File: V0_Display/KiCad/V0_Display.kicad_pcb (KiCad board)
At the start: 2 copper layers, 80 x 35 mm, 28 parts, among them J1 USB_B_Micro, J2 I2C Header 1, J3 Conn_01x03, J4 Conn_01x02, J5 SWD Header, J7 USB_Header, J8 Conn_01x02, SW5 SW_SPST, SW6 SW_SPST, SW7 Rotary_Encoder_Switch, U1 AP2127K-3.3, U2 STM32F042F6Px, U3 74LVC1G17

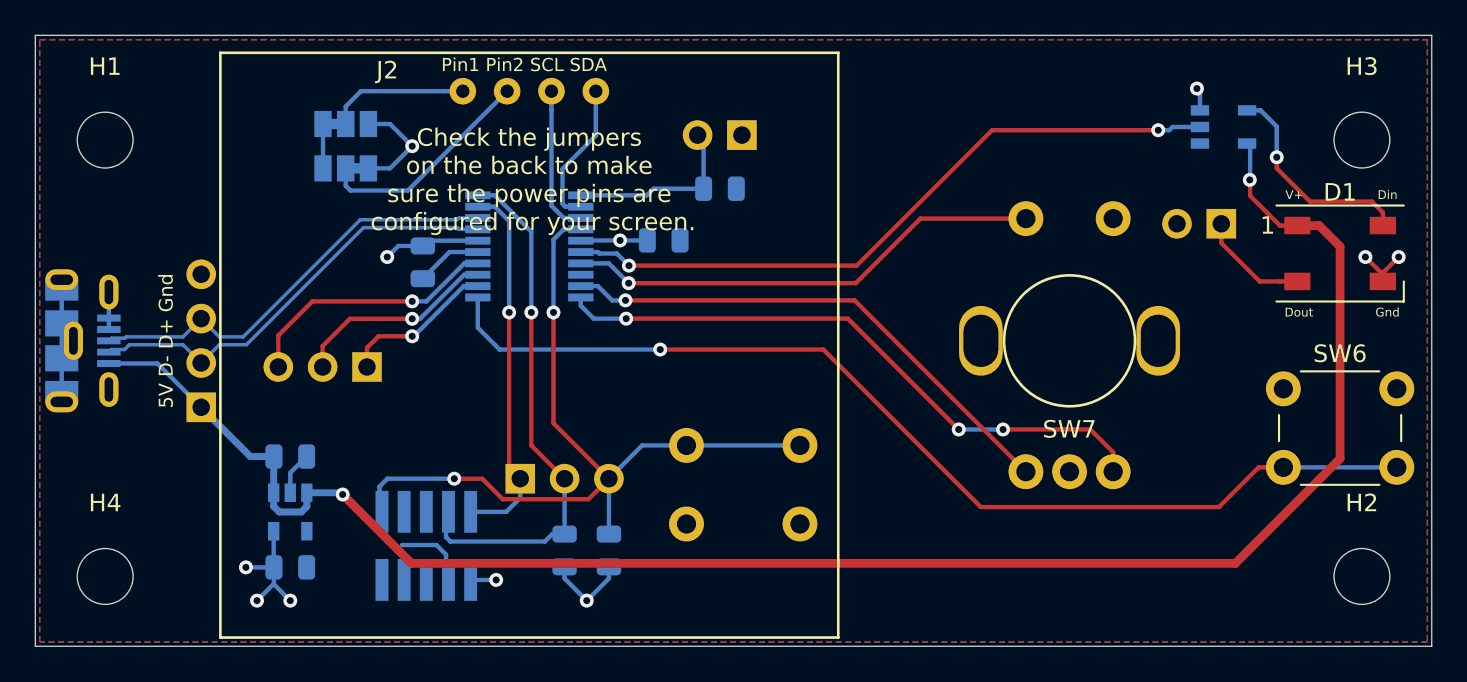
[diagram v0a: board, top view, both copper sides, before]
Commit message: Create Atmega328p version of the V0 Display
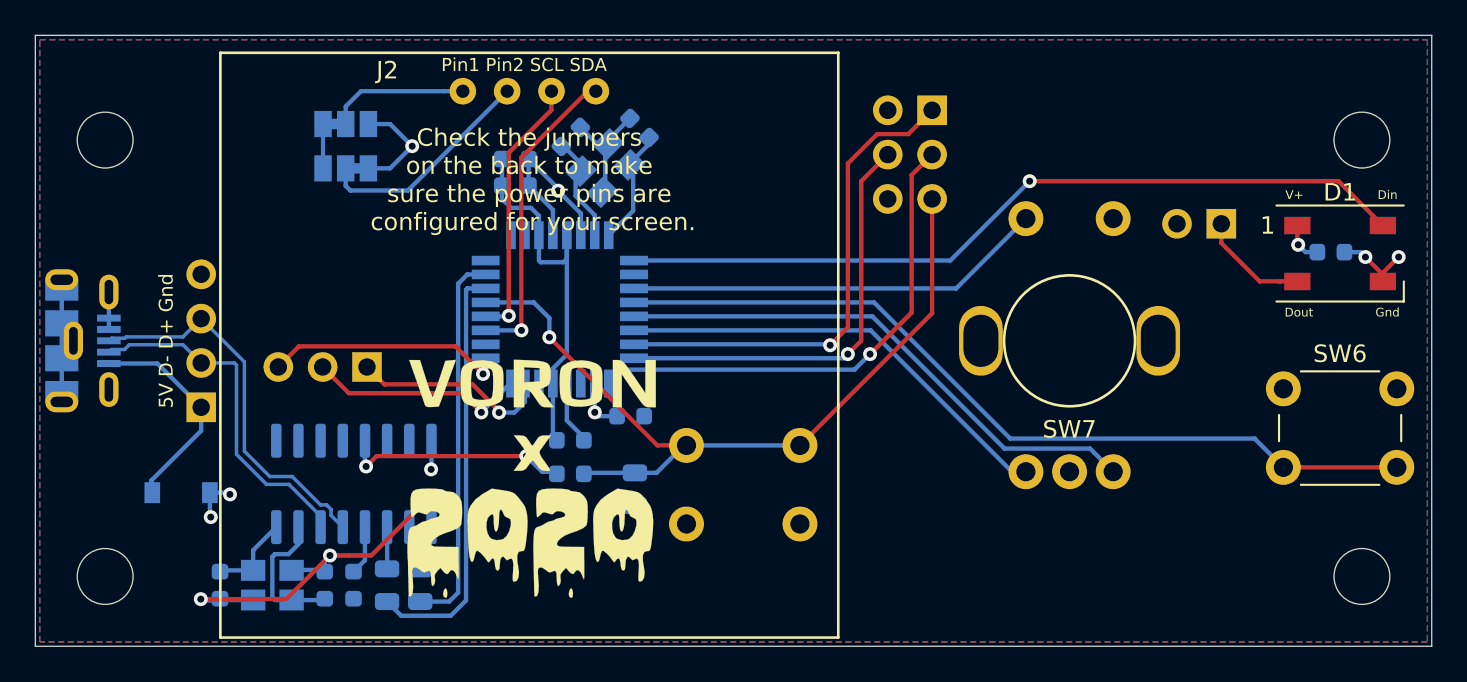
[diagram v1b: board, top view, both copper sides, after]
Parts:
- removed J4: Conn_01x02, V0-Display:PinHeader_1x02_P2.54mm_Vertical
- removed J5: SWD Header, V0-Display:PinHeader_2x05_P1.27mm_Vertical_SMD
- removed R2: 10K, V0-Display:R_0805_2012Metric
- removed U1: AP2127K-3.3, V0-Display:SOT-23-5
- removed U2: STM32F042F6Px, V0-Display:TSSOP-20_4.4x6.5mm_P0.65mm
- removed U3: 74LVC1G17, V0-Display:SOT-753
- added C10: 0.1uF, V0-Display:C_0603_1608Metric, B.Cu at (159.4, 62.1)
- added C11: 0.1uF, V0-Display:C_0603_1608Metric, B.Cu at (103.4, 81.2)
- added C5: 22pF, V0-Display:C_0603_1608Metric, B.Cu at (101.8, 81.2)
- added C6: 22pF, V0-Display:C_0603_1608Metric, B.Cu at (95.8, 81.2)
- added C7: 22pF, V0-Display:C_0603_1608Metric, B.Cu at (119.8, 55.0)
- added C8: 22pF, V0-Display:C_0603_1608Metric, B.Cu at (115.8, 55.5)
- added C9: 0.1uF, V0-Display:C_0603_1608Metric, B.Cu at (119.3, 71.5)
- added D2: 5819, V0-Display:D_SOD-123, B.Cu at (93.5, 75.8)
- added G***: LOGO, V0-Display:2020, F.Cu at (113.7, 74.5)
- added R4: 1K, V0-Display:R_0805_2012Metric, B.Cu at (107.2, 81.2)
- added U4: ATmega328P-AU, V0-Display:TQFP-32_7x7mm_P0.8mm, B.Cu at (115.2, 65.3)
- added U5: CH340G, V0-Display:SOIC-16_3.9x9.9mm_P1.27mm, B.Cu at (103.4, 75.3)
- added Y1: 12MHz, V0-Display:Crystal_SMD_3225-4Pin_3.2x2.5mm, B.Cu at (98.8, 81.2)
- added Y2: 16MHz, V0-Display:Crystal_SMD_3225-4Pin_3.2x2.5mm, B.Cu at (117.8, 57.2)
- C1, C2: value 4.7uF -> 0.1uF; footprint V0-Display:C_0805_2012Metric -> V0-Display:C_0603_1608Metric
- C3, C4: footprint V0-Display:C_0805_2012Metric -> V0-Display:C_0603_1608Metric
- J3: value Conn_01x03 -> ICSP; footprint V0-Display:PinHeader_1x03_P2.54mm_Vertical -> V0-Display:PinHeader_2x03_P2.54mm_Vertical
- R3: value 10K -> 1K
- moved J3 31.7 mm to (136.5, 53.9), turned to 180 degrees
- moved C2 17.6 mm to (115.8, 72.8), turned to 180 degrees
- moved C1 16.1 mm to (115.8, 74.8)
- moved R3 10.4 mm to (105.3, 81.2)
- moved C4 9.06 mm to (112.7, 58.3), turned to 180 degrees
- moved C3 7.94 mm to (112.7, 56.7), turned to 0 degrees
- moved R1 3.82 mm to (119.5, 75.7)
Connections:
- C1 pad 1: VBUS -> Net-(C1-Pad1)
- C1 pad 2: GND -> ~Reset
- C2 pad 1: +3V3 -> Net-(C2-Pad1)
- C3 pad 2: +3V3 -> +5V
- C4 pad 1: +3V3 -> +5V
- D1 pad 1: VBUS -> +5V
- D1 pad 4: Net-(D1-Pad4) -> NeoPixel
- J3 pad 1: SWDIO -> MISO
- J3 pad 2: SWDCLK -> +5V
- J3 pad 3: ~Reset -> SCK
- JP1 pad 1: +3V3 -> +5V
- JP2 pad 3: +3V3 -> +5V
- R1 pad 1: +3V3 -> +5V
- R3 pad 1: +3V3 -> Net-(R3-Pad1)
- R3 pad 2: SWDCLK -> RXD
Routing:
- net VBUS: track 102.4 -> 12.3 mm, vias 2 -> 0
- net GND: track 28.7 -> 85.9 mm, vias 3 -> 5
- net SWDCLK: track 30.6 -> 0.00 mm, vias 1 -> 0
- net +3V3: track 29.3 -> 0.00 mm, vias 8 -> 0
- net SCK: track 0.00 -> 28.6 mm, vias 0 -> 1
- net MISO: track 0.00 -> 28.2 mm, vias 0 -> 1
- net +5V: track 0.00 -> 27.5 mm, vias 0 -> 8
- net MOSI: track 0.00 -> 24.7 mm, vias 0 -> 1
- net Net-(R3-Pad1): track 0.00 -> 24.2 mm
- net Net-(R4-Pad2): track 0.00 -> 21.9 mm
- net SWDIO: track 21.6 -> 0.00 mm, vias 1 -> 0
- net Net-(C1-Pad1): track 0.00 -> 12.9 mm, vias 0 -> 2
- net Net-(D1-Pad4): track 12.4 -> 0.00 mm, vias 1 -> 0
- net Kill_Switch: track 59.6 -> 47.6 mm, vias 1 -> 0
- net BOOT0: track 10.4 -> 0.00 mm
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- added copper zone on F.Cu, net +5V
- removed copper zone on F.Cu, net +3V3
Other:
- board text added: "5V"
- board text added: "GND"
- board text added: "GPIO 1 2 3"
- board text added: "MISO"
- board text added: "MOSI"
- board text added: "SCK"
- board text added: "V0-Display 2020 Shortage Edition B. Lammers Original design by T. Abraham"
- board text removed: "1 2 3 GPIO"
- board text removed: "1 9"
- board text removed: "2 10"
- board text removed: "3V3 BOOT"
- board text removed: "BOOT"
- board text removed: "Reset SWDCLK SWDIO"
- board text removed: "T. Abraham V0-Display Rev-D"
